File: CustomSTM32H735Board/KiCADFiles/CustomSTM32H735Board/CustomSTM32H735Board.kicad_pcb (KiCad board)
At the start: 2 copper layers, 160 x 80 mm, 56 parts, among them J1 Conn_01x03_Socket, J2 Conn_02x10_Odd_Even, J3 FTSH-105-01-L-DV-K, J4 FLE-125-01-G-DV, SW1 SW_Omron_B3FS, U1 STM32H735IGT6, X1 NSC5004A-25M

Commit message: more KiCAD work performed
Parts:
- removed the C13 at (32.5, 20.3)
- added C1: PGB1010603, Capacitor_SMD:C_0603_1608Metric, F.Cu at (76.7, 28.6)
- added C10: 10uF, Capacitor_SMD:C_0805_2012Metric_Pad1.18x1.45mm_HandSolder, F.Cu at (126.0, 146.5)
- added C11: 10uF, Capacitor_SMD:C_0805_2012Metric_Pad1.18x1.45mm_HandSolder, F.Cu at (126.0, 149.6)
- added C14: 1nF, Capacitor_SMD:C_0805_2012Metric_Pad1.18x1.45mm_HandSolder, F.Cu at (126.0, 152.6)
- added C17: 10uF, Capacitor_SMD:C_0805_2012Metric_Pad1.18x1.45mm_HandSolder, F.Cu at (126.0, 158.6)
- added C18: 10uF, Capacitor_SMD:C_0805_2012Metric_Pad1.18x1.45mm_HandSolder, F.Cu at (126.0, 161.6)
- added C19: 4.7uF low ESR, Capacitor_SMD:C_0805_2012Metric_Pad1.18x1.45mm_HandSolder, F.Cu at (130.8, 146.5)
- added C21: PGB1010603, Capacitor_SMD:C_0603_1608Metric, F.Cu at (124.7, 19.6)
- added C22: PGB1010603, Capacitor_SMD:C_0603_1608Metric, F.Cu at (124.7, 22.1)
- added C23: PGB1010603, Capacitor_SMD:C_0603_1608Metric, F.Cu at (124.7, 24.6)
- added C24: 4.7uF low ESR, Capacitor_SMD:C_0805_2012Metric_Pad1.18x1.45mm_HandSolder, F.Cu at (130.8, 149.6)
- added C25: 10uF, Capacitor_SMD:C_0805_2012Metric_Pad1.18x1.45mm_HandSolder, F.Cu at (130.8, 152.6)
- added C26: 100nF, Capacitor_SMD:C_0805_2012Metric_Pad1.18x1.45mm_HandSolder, F.Cu at (130.8, 155.6)
- added C27: 100nF, Capacitor_SMD:C_0805_2012Metric_Pad1.18x1.45mm_HandSolder, F.Cu at (130.8, 158.6)
- added J1: Conn_01x04_Socket, Connector_JST:JST_XH_B4B-XH-A_1x04_P2.50mm_Vertical, F.Cu at (78.2, 22.9)
- added JGPIO1: Conn_01x03_Socket, Connector_JST:JST_XH_B3B-XH-A_1x03_P2.50mm_Vertical, F.Cu at (107.2, 177.8)
- added JP1: SolderJumper_3_Open, Jumper:SolderJumper-3_P1.3mm_Open_Pad1.0x1.5mm_NumberLabels, F.Cu at (106.6, 184.0)
- added JP2: SolderJumper_3_Open, Jumper:SolderJumper-3_P1.3mm_Open_Pad1.0x1.5mm_NumberLabels, F.Cu at (106.6, 187.6)
- added R12: 10k, Resistor_SMD:R_0805_2012Metric_Pad1.20x1.40mm_HandSolder, F.Cu at (101.4, 181.8)
- added R22: 5k1, Resistor_SMD:R_0805_2012Metric_Pad1.20x1.40mm_HandSolder, F.Cu at (101.4, 184.8)
- added R23: 1k, Resistor_SMD:R_0805_2012Metric_Pad1.20x1.40mm_HandSolder, F.Cu at (101.4, 187.7)
- added R3: 10k, Resistor_SMD:R_0805_2012Metric_Pad1.20x1.40mm_HandSolder, F.Cu at (96.6, 175.9)
- added R5: 10k, Resistor_SMD:R_0805_2012Metric_Pad1.20x1.40mm_HandSolder, F.Cu at (96.6, 178.9)
- added R6: 10k, Resistor_SMD:R_0805_2012Metric_Pad1.20x1.40mm_HandSolder, F.Cu at (96.6, 181.8)
- added R7: 10k, Resistor_SMD:R_0805_2012Metric_Pad1.20x1.40mm_HandSolder, F.Cu at (96.6, 184.8)
- added R8: 10k, Resistor_SMD:R_0805_2012Metric_Pad1.20x1.40mm_HandSolder, F.Cu at (96.6, 187.7)
- added R9: 10k, Resistor_SMD:R_0805_2012Metric_Pad1.20x1.40mm_HandSolder, F.Cu at (96.6, 190.7)
- added U2: STM32H735IGT6, Private:LQFP176_STM32H735IGT6_STM-M, F.Cu at (108.9, 159.7)
- C15: value 4.7uF low ESR -> 1nF
- R10: value 5k1 -> 10k
- R11: value R -> 10k
- U1: value STM32H735IGT6 -> OPA1678IDGKT; footprint Private:LQFP176_STM32H735IGT6_STM-M -> Private:OPA1678_L
- moved R10 171.4 mm to (101.4, 175.9)
- moved R11 171.4 mm to (101.4, 178.9)
- moved C15 159.6 mm to (126.0, 155.6)
- moved U1 86.8 mm to (119.0, 176.6)
- renumbered C10 to C12, C11 to C13, C12 to C16, C14 to C20, J1 to J2, JP1 to JP3, J2 to JRadio1, R4 to R13, R5 to R14, R6 to R15, R7 to R16, R8 to R17, R9 to R18, R12 to R19, R13 to R20, R14 to R21, R3 to R4
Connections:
- net /LSBUSB renamed /PD13
- net /RXTX renamed /PD15
- net /S0 renamed /PD12
- net /S1 renamed /PD11
- net /nRXTX renamed /PD14
- C15 pad 1: GND -> Net-(U1B-IN-)
- C15 pad 2: /VDD_SDC -> Net-(U1B-OUT)
- J4 pad 1: unconnected-(J4-Pad1) -> GND
- J4 pad 19: unconnected-(J4-Pad19) -> GND
- J4 pad 2: unconnected-(J4-Pad2) -> GND
- J4 pad 20: unconnected-(J4-Pad20) -> GND
- J4 pad 24: /PG3 -> /PD10
- J4 pad 27: /PD10 -> /PA8
- J4 pad 30: /PE14 -> GND
- J4 pad 32: unconnected-(J4-Pad32) -> /PE14
- J4 pad 34: unconnected-(J4-Pad34) -> GND
- J4 pad 36: unconnected-(J4-Pad36) -> /NRST
- J4 pad 37: unconnected-(J4-Pad37) -> GND
- J4 pad 45: unconnected-(J4-Pad45) -> +3.3V
- J4 pad 47: unconnected-(J4-Pad47) -> GND
- J4 pad 49: unconnected-(J4-Pad49) -> GND
- J4 pad 50: unconnected-(J4-Pad50) -> +3.3V
- JDAC1 pad 2: /DAC1 -> Net-(JDAC1-Pin_2)
- JDAC1 pad 3: /DAC2 -> Net-(JDAC1-Pin_3)
- JI2C1 pad 2: /SDA4 -> /PF15
- JI2C1 pad 3: /SCL4 -> /PF14
- JI2C2 pad 2: /SDA2 -> /PB11
- JI2C2 pad 3: /SCL2 -> /PB10
- JI2C3 pad 2: /SDA1 -> /PB7
- JI2C3 pad 3: /SCL1 -> /PB6
- JP3 pad 3: Net-(JP1-B) -> Net-(JP3-B)
- JRadio1 pad 17: /R_CH1 -> /PF6
- JRadio1 pad 18: /R_CH2 -> /PF7
- JRadio1 pad 19: /ADC1 -> /PF11
- JRadio1 pad 20: /ADC2 -> /PF13
- JUART1 pad 2: /UART_RX -> /PC11
- JUART1 pad 3: /UART_TX -> /PA0
- R10 pad 1: /BOOT0 -> GND
- R10 pad 2: GND -> Net-(U1B-IN+)
- R11 pad 1: /PDR_ON -> Net-(U1A-OUT)
- R11 pad 2: +3.3V -> Net-(U1A-IN-)
- R13 pad 1: /SDA4 -> /PF15
- R14 pad 1: /SDA2 -> /PB11
- R15 pad 1: /SDA1 -> /PB7
- R16 pad 1: /SCL4 -> /PF14
- R17 pad 1: /SCL2 -> /PB10
- R18 pad 1: /SCL1 -> /PB6
- U1 pad 1: /PE2 -> Net-(U1A-OUT)
- U1 pad 2: unconnected-(U1-Pad2) -> Net-(U1A-IN-)
- U1 pad 3: /PE4 -> Net-(U1A-IN+)
- U1 pad 4: /PE5 -> -5V
- U1 pad 5: /PE6 -> Net-(U1B-IN+)
- U1 pad 6: GND -> Net-(U1B-IN-)
- U1 pad 7: +3.3V -> Net-(U1B-OUT)
- U1 pad 8: +3.3V -> +5V
- UFLASH1 pad A5: /PG6 -> Net-(UFLASH1-~{ECS})
- UFLASH1 pad E3: /PC2_C -> /PE8

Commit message: finished schematics, check with AS performed
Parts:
- removed H5, H6, H7, H8: MountingHole_Pad_MP, MountingHole:MountingHole_2.7mm_M2.5_Pad_TopBottom
- removed the J1 at (78.2, 22.9)
- added C1: 47uF Tant. 25V, Capacitor_Tantalum_SMD:CP_EIA-7343-30_AVX-N_Pad2.25x2.55mm_HandSolder, F.Cu at (72.4, 119.0)
- added C13: 100uF Tant. 25V, Capacitor_Tantalum_SMD:CP_EIA-7343-30_AVX-N_Pad2.25x2.55mm_HandSolder, F.Cu at (122.7, 128.0)
- added C15: 1uF, Capacitor_SMD:C_0805_2012Metric_Pad1.18x1.45mm_HandSolder, F.Cu at (84.6, 130.3)
- added C17: 100nF, Capacitor_SMD:C_0805_2012Metric_Pad1.18x1.45mm_HandSolder, F.Cu at (98.0, 130.7)
- added C19: 10uF Tant. 25V, Capacitor_Tantalum_SMD:CP_EIA-7343-30_AVX-N_Pad2.25x2.55mm_HandSolder, F.Cu at (94.0, 128.0)
- added C2: 10uF Tant. 25V, Capacitor_Tantalum_SMD:CP_EIA-7343-30_AVX-N_Pad2.25x2.55mm_HandSolder, F.Cu at (106.7, 124.2)
- added C3: 100nF, Capacitor_SMD:C_0805_2012Metric_Pad1.18x1.45mm_HandSolder, F.Cu at (72.4, 126.0)
- added C4: optional: 82pF, Capacitor_SMD:C_0805_2012Metric_Pad1.18x1.45mm_HandSolder, F.Cu at (101.5, 130.7)
- added C5: 100nF, Capacitor_SMD:C_0805_2012Metric_Pad1.18x1.45mm_HandSolder, F.Cu at (80.3, 130.3)
- added C6: 47uF Tant. 25V, Capacitor_Tantalum_SMD:CP_EIA-7343-30_AVX-N_Pad2.25x2.55mm_HandSolder, F.Cu at (88.9, 123.2)
- added C7: 1uF, Tant. 25V, Capacitor_Tantalum_SMD:CP_EIA-7343-30_AVX-N_Pad2.25x2.55mm_HandSolder, F.Cu at (114.6, 123.2)
- added D1: PMEG2010AEH, Diode_SMD:D_SOD-123F, F.Cu at (112.1, 130.4)
- added IC1: NCP700BSN33T1G, Private:SOT95P275X120-5N, F.Cu at (89.1, 130.4)
- added JPOWER1: Conn_01x02_Socket, Connector_JST:JST_XH_B2B-XH-A_1x02_P2.50mm_Vertical, B.Cu at (64.8, 117.3)
- added L1: 10uH, Inductor_SMD:L_1812_4532Metric_Pad1.30x3.40mm_HandSolder, F.Cu at (116.7, 130.0)
- added PS1: TPS6735ID, Private:SOIC127P600X175-8N, F.Cu at (107.0, 129.8)
- added U1: L7805, Package_TO_SOT_THT:TO-220-3_Horizontal_TabDown, F.Cu at (78.2, 126.6)
- H1, H2, H3, H4: value MountingHole_Pad_MP -> MountingHole_Pad; footprint MountingHole:MountingHole_2.7mm_M2.5_Pad_TopBottom -> MountingHole:MountingHole_3.2mm_M3_Pad_TopBottom
- J1: renamed from J2; footprint Connector_JST:JST_XH_B2B-XH-AM_1x02_P2.50mm_Vertical -> Connector_JST:JST_XH_B3B-XH-A_1x03_P2.50mm_Vertical; moved to B.Cu
- JADC1: footprint Connector_JST:JST_XH_B3B-XH-A_1x03_P2.50mm_Vertical -> Connector_JST:JST_XH_B2B-XH-A_1x02_P2.50mm_Vertical; moved to B.Cu
- JDAC1, JGPIO1, JI2C1, JI2C2, JI2C3, JUART1, UFLASH1: moved to B.Cu
- moved JDAC1 176.6 mm to (66.3, 86.1), turned to 180 degrees
- moved JI2C2 173.7 mm to (69.0, 100.6), turned to 180 degrees
- moved JUART1 172.5 mm to (69.0, 108.0), turned to 180 degrees
- moved H3 160.2 mm to (65.5, 128.3)
- moved JI2C1 147.1 mm to (93.9, 78.7), turned to 180 degrees
- moved H2 140.0 mm to (181.9, 72.1)
- moved JI2C3 134.3 mm to (105.8, 77.0), turned to 180 degrees
- moved J1 102.3 mm to (171.7, 128.0), turned to 180 degrees
- moved JP2 99.4 mm to (156.4, 101.6)
- moved R11 99.4 mm to (151.2, 92.9)
- moved R12 99.4 mm to (151.2, 95.8)
- moved R23 99.4 mm to (151.2, 101.7)
- moved R5 99.4 mm to (146.5, 92.9)
- moved R6 99.4 mm to (146.5, 95.8)
- moved R8 99.4 mm to (146.5, 101.7)
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- renumbered C3 to C10, C4 to C11, C5 to C12, C6 to C14, C7 to C16, C8 to C18, C9 to C20, C10 to C21, C11 to C22, C12 to C23, C13 to C24, C14 to C25, C15 to C26, C16 to C27, C17 to C28, C18 to C29, C19 to C30, C20 to C31, C21 to C32, C22 to C33, C23 to C34, C24 to C35, C25 to C36, C26 to C37, C27 to C38, C1 to C8, C2 to C9, J3 to J2, J4 to J3, L1 to L2, U1 to U2, U2 to U3
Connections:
- C11 pad 1: +3.3V -> /VDD
- C16 pad 1: +3.3V -> /VDD
- C20 pad 1: +3.3V -> /VDD
- C36 pad 1: +3.3V -> +5V
- C37 pad 1: +3.3V -> +5V
- FB1 pad 1: +3.3V -> /VDD
- H1 pad 1: (no net) -> GND
- H2 pad 1: (no net) -> GND
- H3 pad 1: (no net) -> GND
- H4 pad 1: (no net) -> GND
- J3 pad 45: +3.3V -> +5V
- JP3 pad 1: +3.3V -> /VDD
- U3 pad 100: GND -> /VSS
- U3 pad 105: +3.3V -> /VDD
- U3 pad 106: GND -> /VSS
- U3 pad 112: GND -> /VSS
- U3 pad 113: +3.3V -> /VDD
- U3 pad 119: GND -> /VSS
- U3 pad 12: GND -> /VSS
- U3 pad 121: GND -> /VSS
- U3 pad 126: +3.3V -> /VDD
- U3 pad 13: +3.3V -> /VDD
- U3 pad 134: GND -> /VSS
- U3 pad 136: +3.3V -> /VDD
- U3 pad 137: GND -> /VSS
- U3 pad 151: GND -> /VSS
- U3 pad 152: +3.3V -> /VDD
- U3 pad 159: GND -> /VSS
- U3 pad 160: +3.3V -> /VDD
- U3 pad 173: GND -> /VSS
- U3 pad 176: +3.3V -> /VDD
- U3 pad 24: GND -> /VSS
- U3 pad 25: +3.3V -> /VDD
- U3 pad 38: GND -> /VSS
- U3 pad 44: +3.3V -> /VDD
- U3 pad 45: GND -> /VSS
- U3 pad 47: GND -> /VSS
- U3 pad 48: +3.3V -> /VDD
- U3 pad 6: GND -> /VSS
- U3 pad 64: GND -> /VSS
- U3 pad 65: +3.3V -> /VDD
- U3 pad 7: +3.3V -> /VDD
- U3 pad 70: GND -> /VSS
- U3 pad 71: +3.3V -> /VDD
- U3 pad 8: +3.3V -> /VDD
- U3 pad 81: GND -> /VSS
- U3 pad 83: GND -> /VSS
- U3 pad 84: +3.3V -> /VDD
- U3 pad 92: +3.3V -> /VDD
- U3 pad 93: GND -> /VSS
- U3 pad 99: +3.3V -> /VDD
- UHYPERRAM1 pad B3: GND -> /VSS
- UHYPERRAM1 pad B4: +3.3V -> /VDD
- UHYPERRAM1 pad C1: GND -> /VSS
- UHYPERRAM1 pad D1: +3.3V -> /VDD
- UHYPERRAM1 pad E4: +3.3V -> /VDD
- UHYPERRAM1 pad E5: GND -> /VSS
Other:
- board size 160 x 80 mm -> 127 x 73 mm

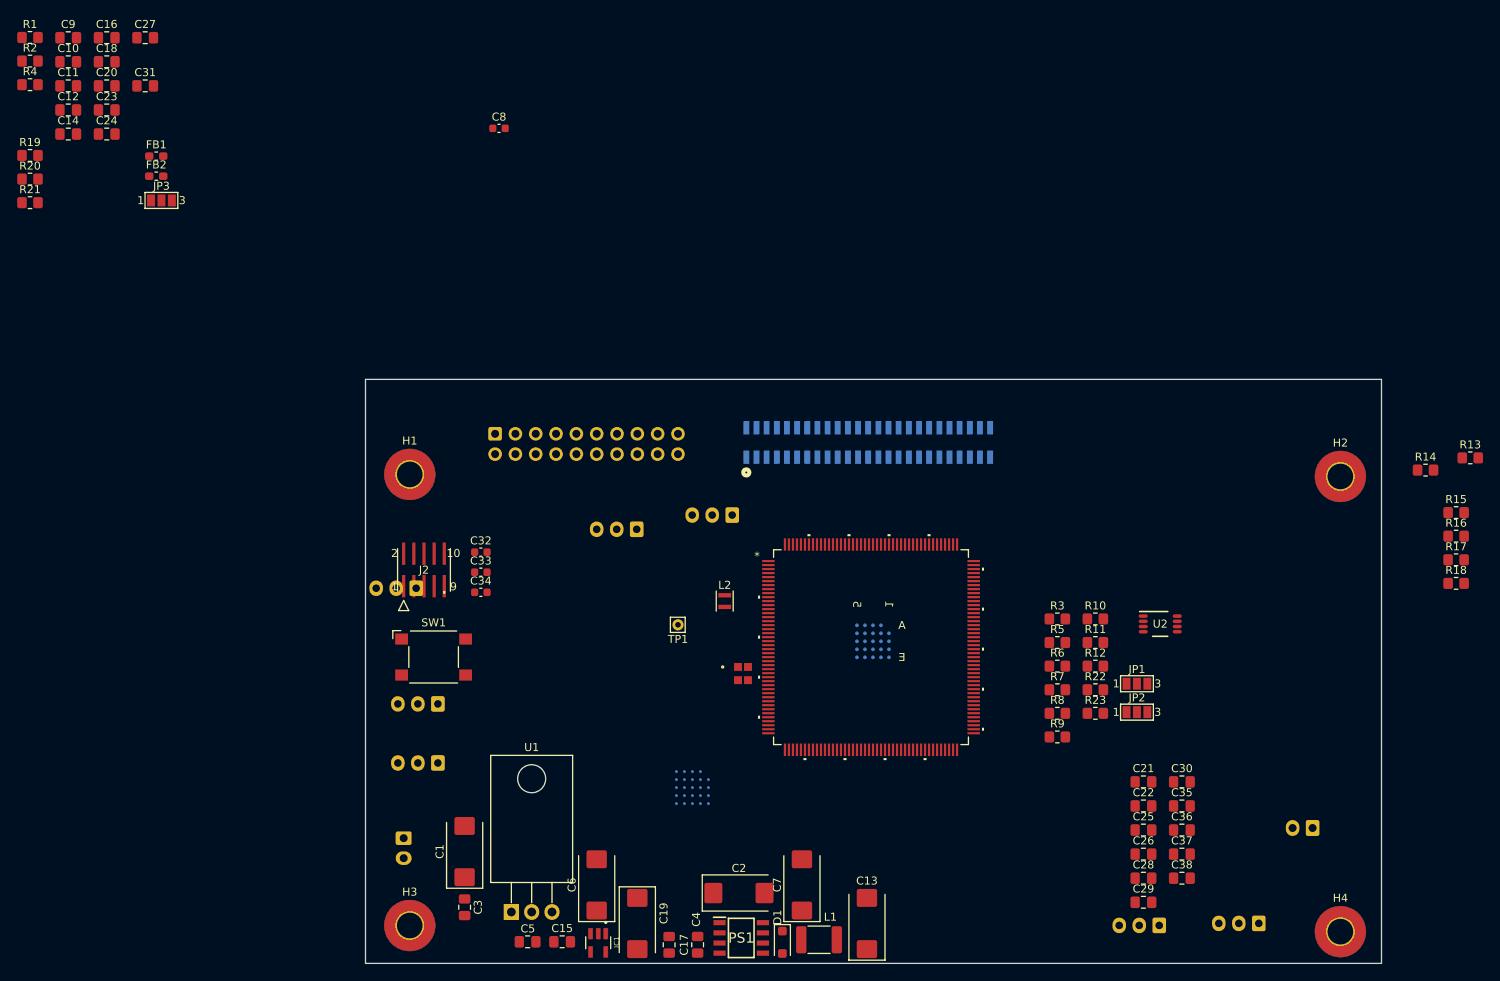
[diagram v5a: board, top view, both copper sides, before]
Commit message: Layout finished. Started with board design of custom board.
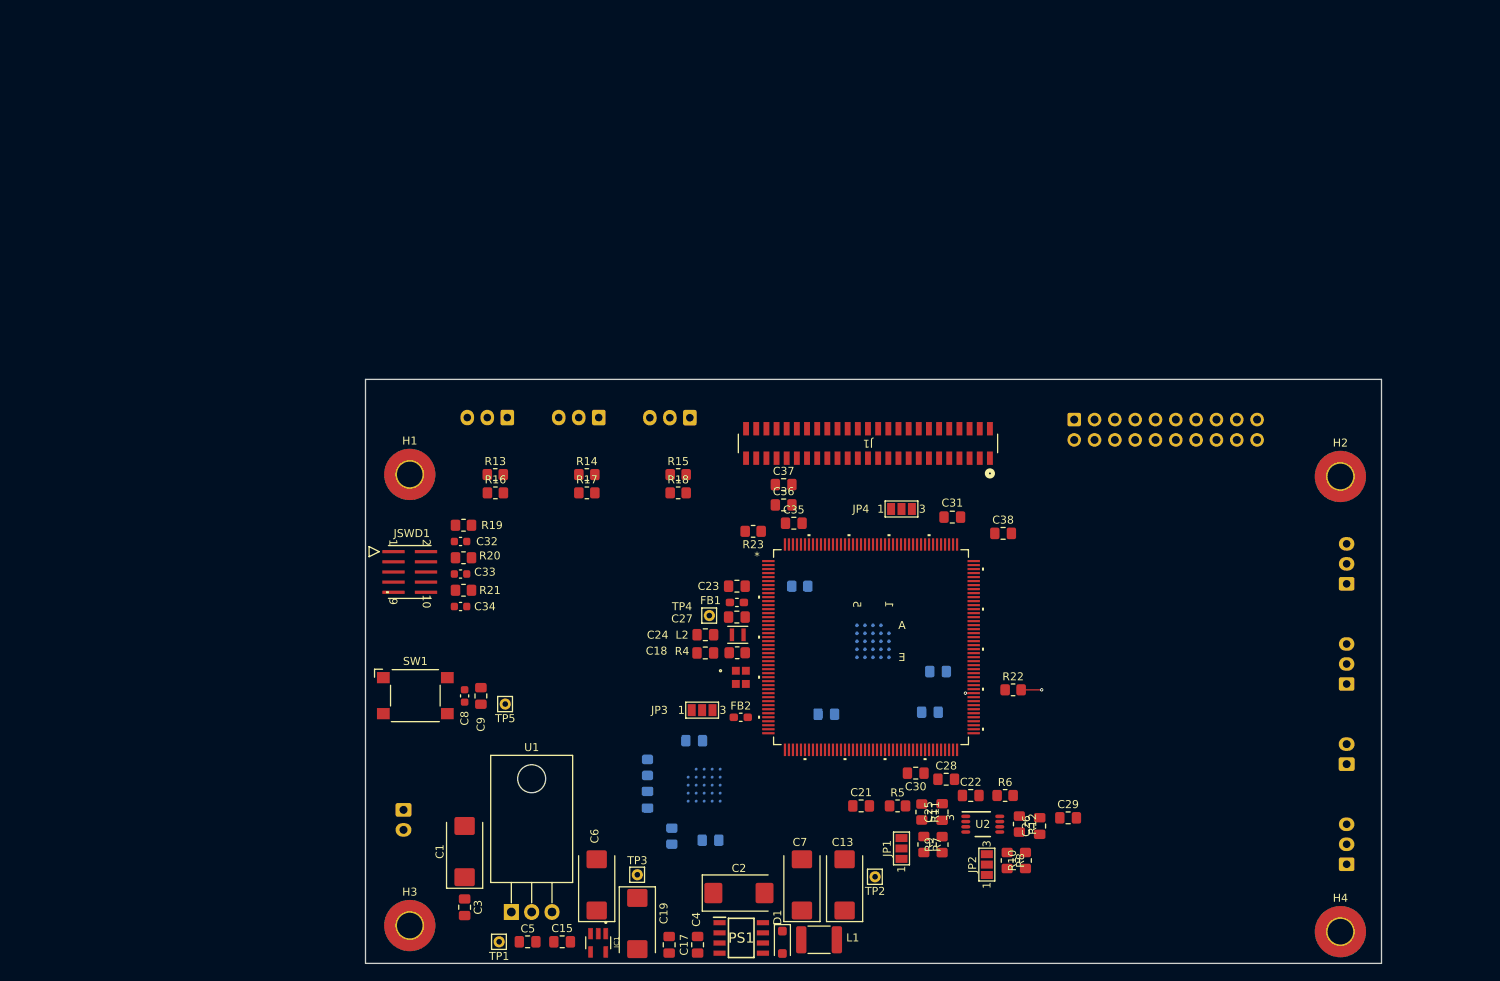
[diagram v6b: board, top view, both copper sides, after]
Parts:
- removed the J1 at (171.7, 128.0)
- added JP4: SolderJumper_3_Open, Jumper:SolderJumper-3_P1.3mm_Open_Pad1.0x1.5mm_NumberLabels, F.Cu at (127.0, 76.2)
- added TP1: TestPoint, Connector_Pin:Pin_D0.7mm_L6.5mm_W1.8mm_FlatFork, F.Cu at (76.7, 130.3)
- added TP2: TestPoint, Connector_Pin:Pin_D0.7mm_L6.5mm_W1.8mm_FlatFork, F.Cu at (123.7, 122.2)
- added TP3: TestPoint, Connector_Pin:Pin_D0.7mm_L6.5mm_W1.8mm_FlatFork, F.Cu at (94.0, 121.9)
- added TP5: TestPoint, Connector_Pin:Pin_D0.7mm_L6.5mm_W1.8mm_FlatFork, F.Cu at (77.5, 100.6)
- C10: renamed from C9; moved to B.Cu
- C11, C12, C14, C16, C20, R1, R2, R3: moved to B.Cu
- J1: renamed from J3; moved to F.Cu
- moved C16 133.0 mm to (130.6, 101.6), turned to 180 degrees
- moved C10 128.5 mm to (103.1, 117.6), turned to 180 degrees
- moved C20 127.1 mm to (131.6, 96.5), turned to 180 degrees
- moved C11 123.1 mm to (117.6, 101.9), turned to 180 degrees
- moved R13 121.9 mm to (76.2, 71.9)
- moved R16 120.2 mm to (76.2, 74.2)
- moved R1 118.2 mm to (114.3, 85.9), turned to 180 degrees
- moved R2 117.3 mm to (95.2, 108.5), turned to -90 degrees
- moved JDAC1 116.9 mm to (182.6, 98.1), turned to 90 degrees
- moved JUART1 115.8 mm to (182.6, 85.6), turned to 90 degrees
- moved C31 114.4 mm to (133.3, 77.2), turned to 180 degrees
- moved R4 113.4 mm to (106.5, 94.2), turned to 180 degrees
- moved C12 112.6 mm to (95.2, 112.5), turned to 90 degrees
- moved R17 109.0 mm to (87.7, 74.2)
- moved C14 109.0 mm to (101.1, 105.2), turned to 180 degrees
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- renumbered C10 to C9, J2 to JSWD1, TP1 to TP4
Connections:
- C11 pad 1: /VDD -> +3.3V
- C16 pad 1: /VDD -> +3.3V
- C20 pad 1: /VDD -> +3.3V
- FB1 pad 1: /VDD -> +3.3V
- J1 pad 36: /NRST -> Net-(JP4-C)
- JP3 pad 1: /VDD -> +3.3V
- U3 pad 100: /VSS -> GND
- U3 pad 105: /VDD -> +3.3V
- U3 pad 106: /VSS -> GND
- U3 pad 112: /VSS -> GND
- U3 pad 113: /VDD -> +3.3V
- U3 pad 119: /VSS -> GND
- U3 pad 12: /VSS -> GND
- U3 pad 121: /VSS -> GND
- U3 pad 126: /VDD -> +3.3V
- U3 pad 13: /VDD -> +3.3V
- U3 pad 134: /VSS -> GND
- U3 pad 136: /VDD -> +3.3V
- U3 pad 137: /VSS -> GND
- U3 pad 139: /PC15 -> /PA15
- U3 pad 143: unconnected-(U3-Pad143) -> /PD0
- U3 pad 151: /VSS -> GND
- U3 pad 152: /VDD -> +3.3V
- U3 pad 159: /VSS -> GND
- U3 pad 160: /VDD -> +3.3V
- U3 pad 173: /VSS -> GND
- U3 pad 176: /VDD -> +3.3V
- U3 pad 24: /VSS -> GND
- U3 pad 25: /VDD -> +3.3V
- U3 pad 38: /VSS -> GND
- U3 pad 44: /VDD -> +3.3V
- U3 pad 45: /VSS -> GND
- U3 pad 47: /VSS -> GND
- U3 pad 48: /VDD -> +3.3V
- U3 pad 6: /VSS -> GND
- U3 pad 64: /VSS -> GND
- U3 pad 65: /VDD -> +3.3V
- U3 pad 7: /VDD -> +3.3V
- U3 pad 70: /VSS -> GND
- U3 pad 71: /VDD -> +3.3V
- U3 pad 8: /VDD -> +3.3V
- U3 pad 81: /VSS -> GND
- U3 pad 83: /VSS -> GND
- U3 pad 84: /VDD -> +3.3V
- U3 pad 92: /VDD -> +3.3V
- U3 pad 93: /VSS -> GND
- U3 pad 99: /VDD -> +3.3V
- UHYPERRAM1 pad B3: /VSS -> GND
- UHYPERRAM1 pad B4: /VDD -> +3.3V
- UHYPERRAM1 pad C1: /VSS -> GND
- UHYPERRAM1 pad D1: /VDD -> +3.3V
- UHYPERRAM1 pad E4: /VDD -> +3.3V
- UHYPERRAM1 pad E5: /VSS -> GND
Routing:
- net GND: track 0.00 -> 2.57 mm, vias 0 -> 1
- net +3.3V: track 0.00 -> 1.04 mm, vias 0 -> 1
- added copper zone on In2.Cu, net +3.3V
- added copper zone on In1.Cu, net GND
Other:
- copper layers 2 -> 4
